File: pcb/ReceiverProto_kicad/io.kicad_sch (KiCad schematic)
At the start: 4 parts, among them J1 Conn_01x09, J2 Conn_01x03, J3 Conn_01x03, J4 Conn_01x06

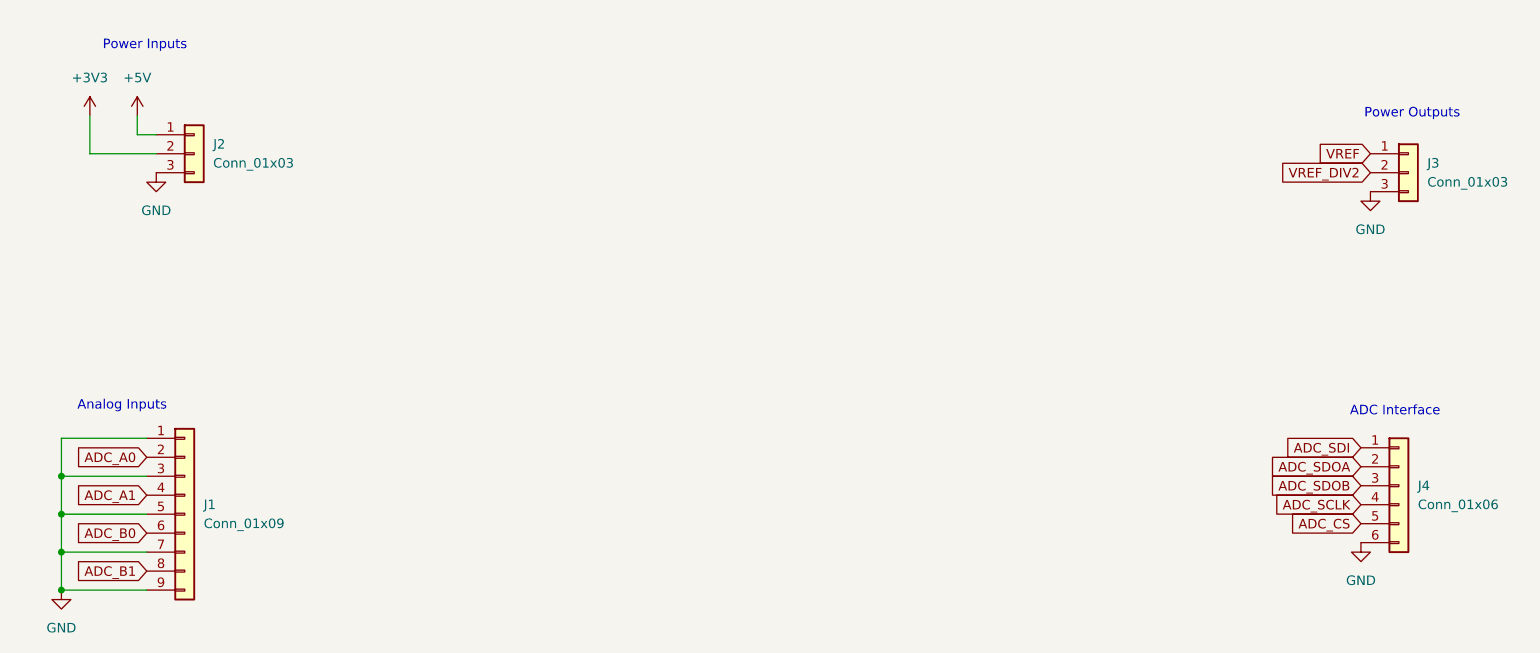
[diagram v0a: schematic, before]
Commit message: add footprints for remaining symbols; 3.3V regulator still needs footprint
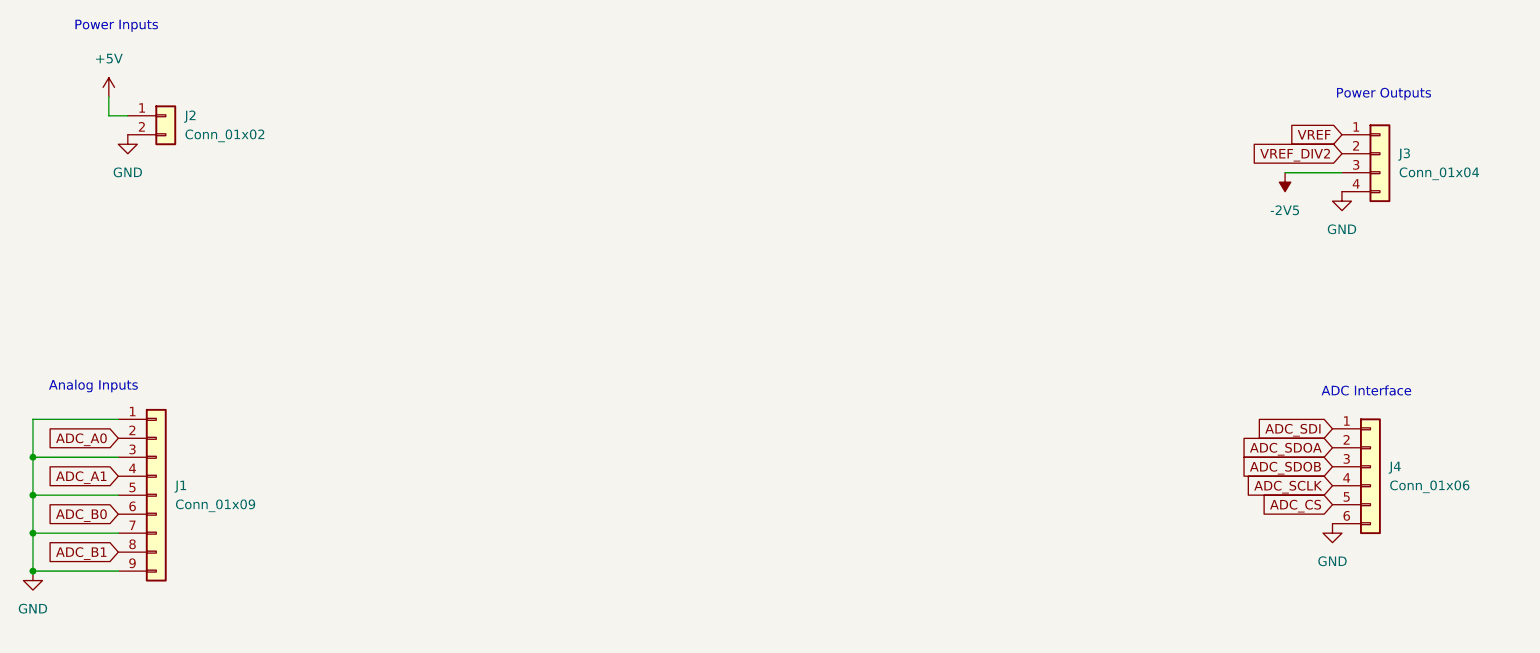
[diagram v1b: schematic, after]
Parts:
- removed J2, J3: Conn_01x03, symbol Connector_Generic:Conn_01x03
- added J2: Conn_01x02, Connector_PinHeader_2.54mm:PinHeader_1x02_P2.54mm_Vertical, symbol Connector_Generic:Conn_01x02
- added J3: Conn_01x04, Connector_PinHeader_2.54mm:PinHeader_1x04_P2.54mm_Vertical, symbol Connector_Generic:Conn_01x04
- J1: footprint (none) -> Connector_PinHeader_2.54mm:PinHeader_1x09_P2.54mm_Vertical
- J4: footprint (none) -> Connector_PinHeader_2.54mm:PinHeader_1x06_P2.54mm_Vertical
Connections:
- net +5V: now also J2.1 (Pin_1)
- net GND: now also J2.2 (Pin_2), J3.4 (Pin_4)
- net VREF: now also J3.1 (Pin_1)
- net VREF_DIV2: now also J3.2 (Pin_2)
- new net -2V5: J3.3 (Pin_3)
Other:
- moved on the sheet: J1, J4

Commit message: Fixed footprint for voltage regulator.
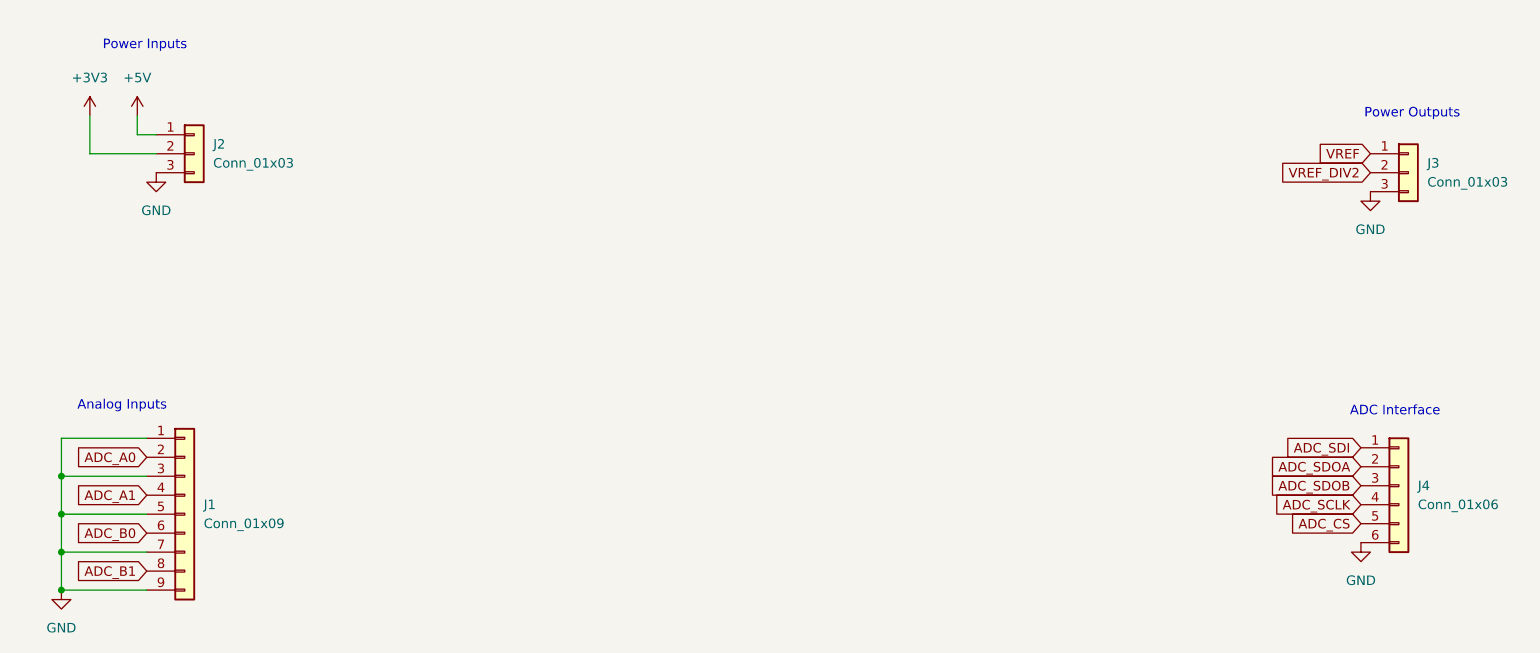
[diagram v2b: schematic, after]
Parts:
- removed J2: Conn_01x02, Connector_PinHeader_2.54mm:PinHeader_1x02_P2.54mm_Vertical, symbol Connector_Generic:Conn_01x02
- removed J3: Conn_01x04, Connector_PinHeader_2.54mm:PinHeader_1x04_P2.54mm_Vertical, symbol Connector_Generic:Conn_01x04
- added J2, J3: Conn_01x03, symbol Connector_Generic:Conn_01x03
- J1: footprint Connector_PinHeader_2.54mm:PinHeader_1x09_P2.54mm_Vertical -> (none)
- J4: footprint Connector_PinHeader_2.54mm:PinHeader_1x06_P2.54mm_Vertical -> (none)
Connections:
- net +5V: now also J2.1 (Pin_1)
- net GND: now also J2.3 (Pin_3), J3.3 (Pin_3)
- net VREF: now also J3.1 (Pin_1)
- net VREF_DIV2: now also J3.2 (Pin_2)
- new net +3V3: J2.2 (Pin_2)
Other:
- moved on the sheet: J1, J4
